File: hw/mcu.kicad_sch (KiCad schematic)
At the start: 40 parts, among them J3 Wisevision N114-2413THBIG01-H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, J4 Prog/debug, J5 Conn_02x04_Odd_Even, Q3 AO3401A, Q4 2N7002, Q5 2N7002, SW1 SW_Push_Shielded, SW2 SW_Push_Shielded, SW3 SW_Push_Shielded, SW8 SW_Push, U5 STM32L496RETx, U6 ZD25WQ16CTIGT, U7 PAM2804, Y1 32768 Hz

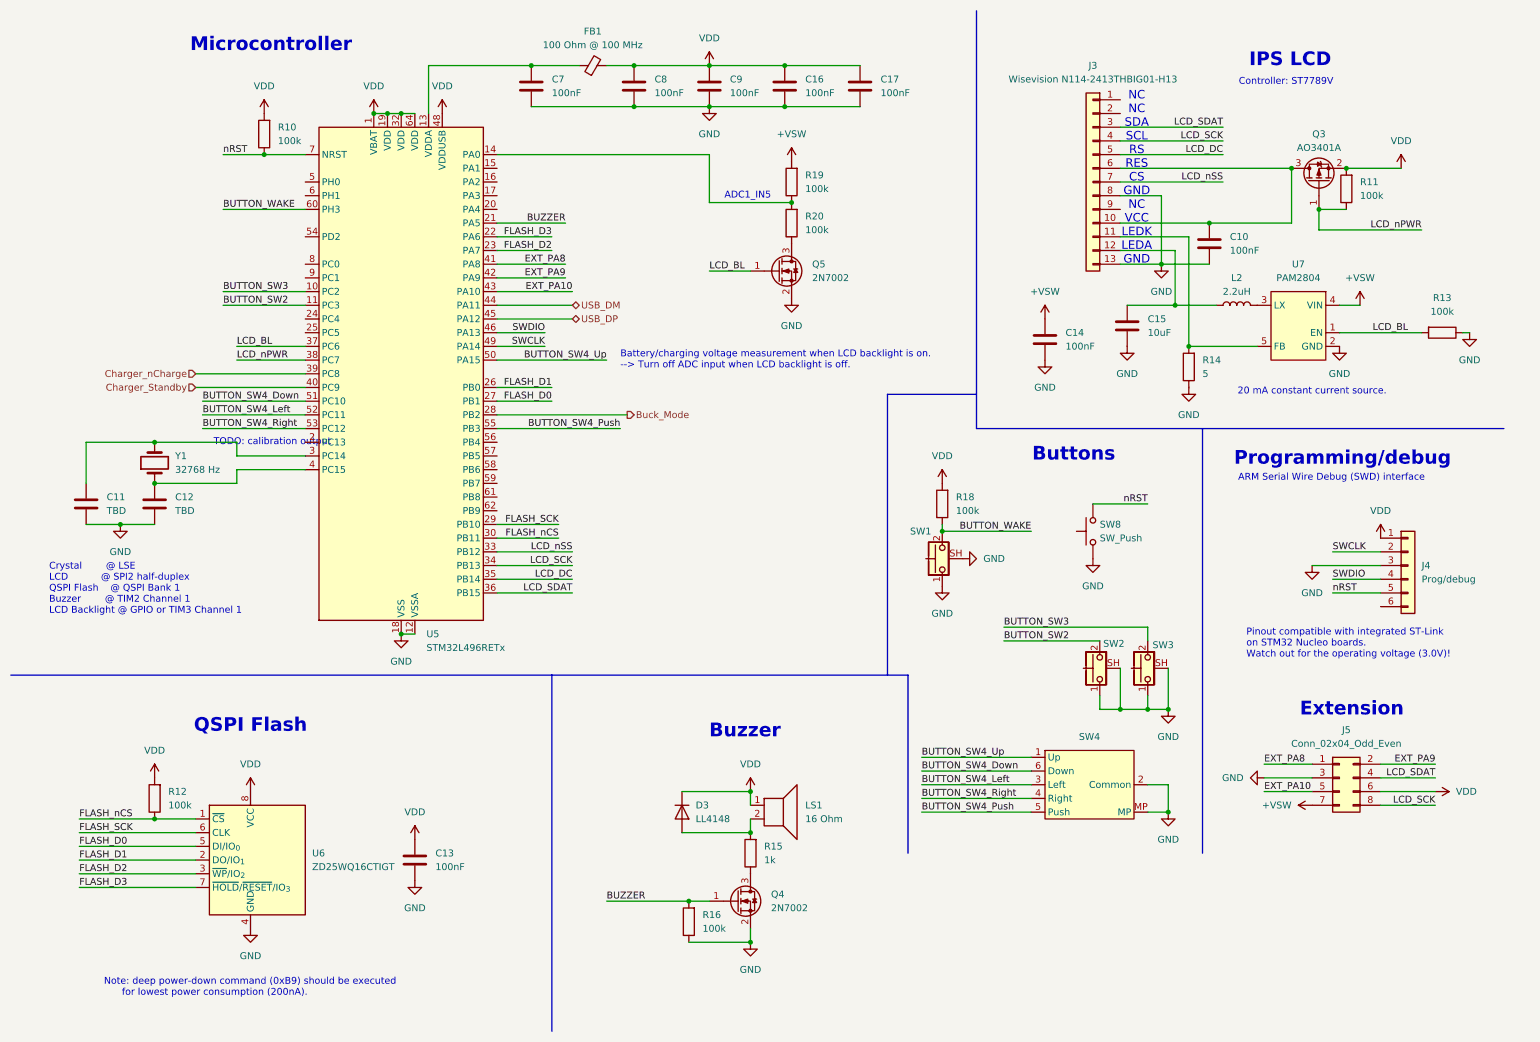
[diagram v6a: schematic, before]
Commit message: Placed remaining components.
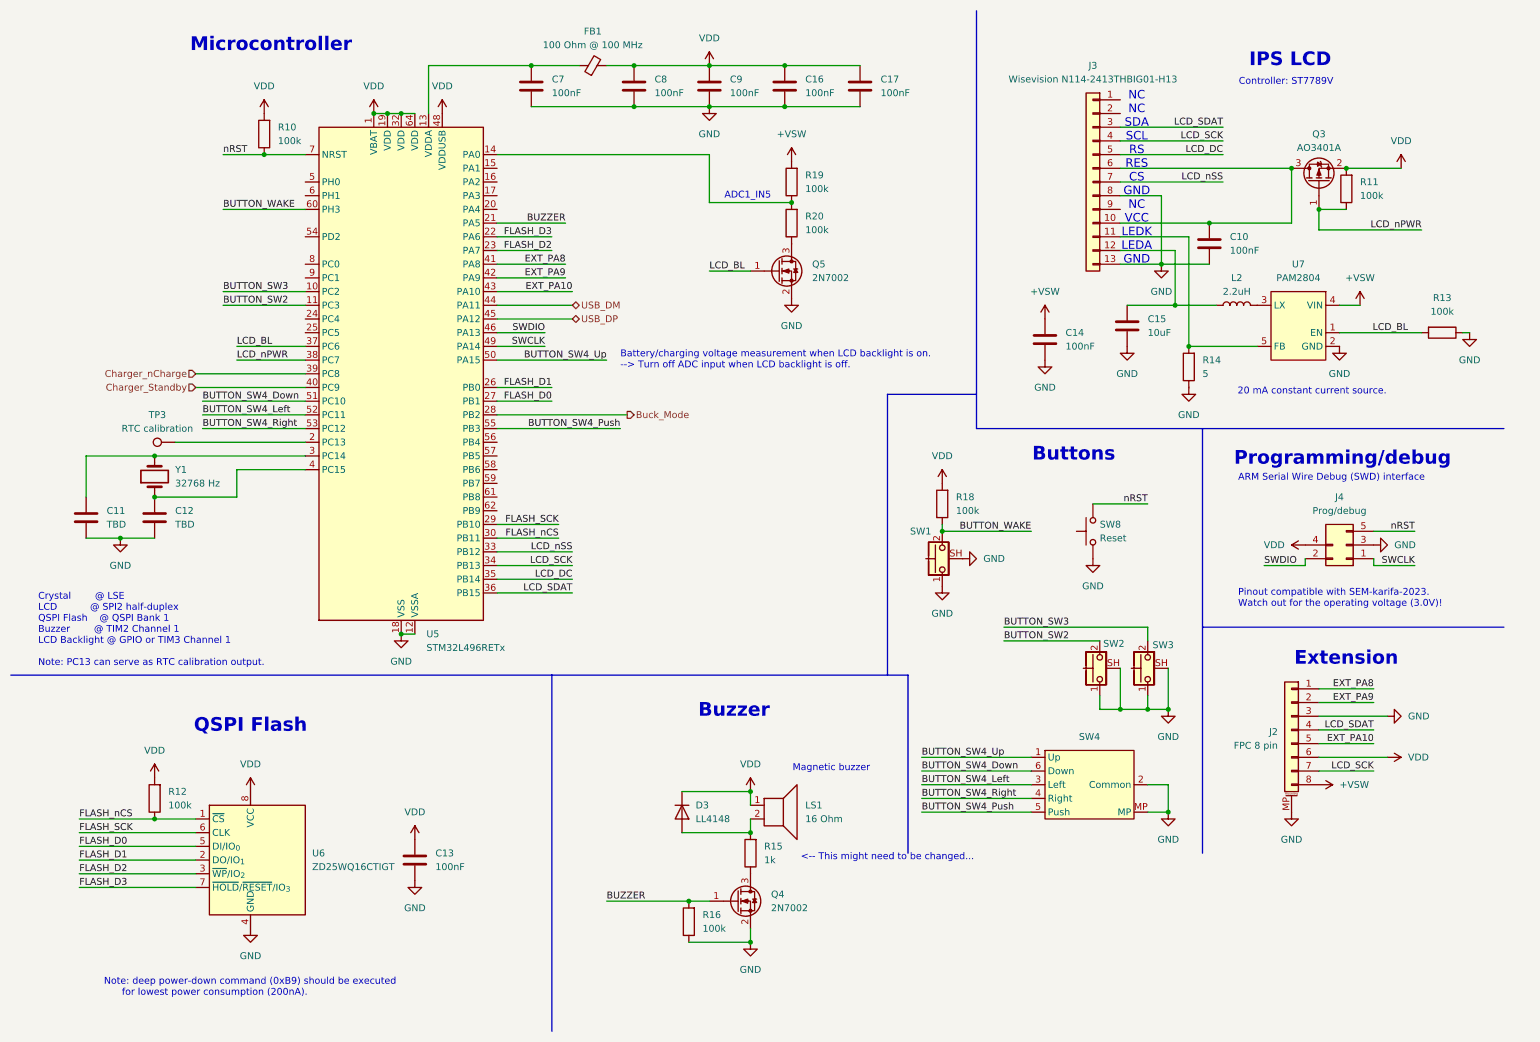
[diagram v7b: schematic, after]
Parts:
- removed J4: Prog/debug, Connector_PinHeader_2.54mm:PinHeader_1x06_P2.54mm_Vertical, symbol Connector_Generic:Conn_01x06
- removed J5: Conn_02x04_Odd_Even, Connector_PinHeader_2.54mm:PinHeader_2x04_P2.54mm_Vertical, symbol Connector_Generic:Conn_02x04_Odd_Even
- added J2: FPC 8 pin, Connector_FFC-FPC:Hirose_FH12-8S-0.5SH_1x08-1MP_P0.50mm_Horizontal, symbol Connector_Generic_MountingPin:Conn_01x08_MountingPin
- added J4: Prog/debug, sem18:ProgConnector_5pin, symbol Connector_Generic:Conn_2Rows-05Pins
- added TP3: RTC calibration, TestPoint:TestPoint_Pad_D1.0mm, symbol Connector:TestPoint
- LS1: footprint Buzzer_Beeper:MagneticBuzzer_CUI_CMT-8504-100-SMT -> sem18:Buzzer_8.5x8.5mm
- SW8: value SW_Push -> Reset; footprint (none) -> Button_Switch_SMD:SW_SPST_TL3342
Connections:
- net +VSW: now also J2.8 (Pin_8)
- net EXT_PA10: now also J2.5 (Pin_5)
- net EXT_PA8: now also J2.1 (Pin_1)
- net EXT_PA9: now also J2.2 (Pin_2)
- net GND: now also J2.3 (Pin_3), J2.MP (MountPin), J4.3 (Pin_3)
- net LCD_SCK: now also J2.7 (Pin_7)
- net LCD_SDAT: now also J2.4 (Pin_4)
- net SWCLK: now also J4.1 (Pin_1)
- net SWDIO: now also J4.2 (Pin_2)
- net VDD: now also J2.6 (Pin_6), J4.4 (Pin_4)
- net nRST: now also J4.5 (Pin_5)
- net at U5.2 (PC13): now also TP3.1
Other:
- note added: "<-- This might need to be changed..."
- note added: "Crystal @ LSE LCD @ SPI2 half-duplex QSPI Flash @ QSPI Bank 1 Buzzer @ TIM2 Channel 1 LCD Backlight @ GPIO or TIM3 Channel 1 Note: PC13 can serve as RTC calibration output."
- note added: "Magnetic buzzer"
- note added: "Pinout compatible with SEM-karifa-2023. Watch out for the operating voltage (3.0V)!"
- note removed: "Crystal @ LSE LCD @ SPI2 half-duplex QSPI Flash @ QSPI Bank 1 Buzzer @ TIM2 Channel 1 LCD Backlight @ GPIO or TIM3 Channel 1"
- note removed: "Pinout compatible with integrated ST-Link on STM32 Nucleo boards. Watch out for the operating voltage (3.0V)!"
- note removed: "TODO: calibration output"
- moved on the sheet: C11, C12, Y1

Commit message: Replaced extension connector.
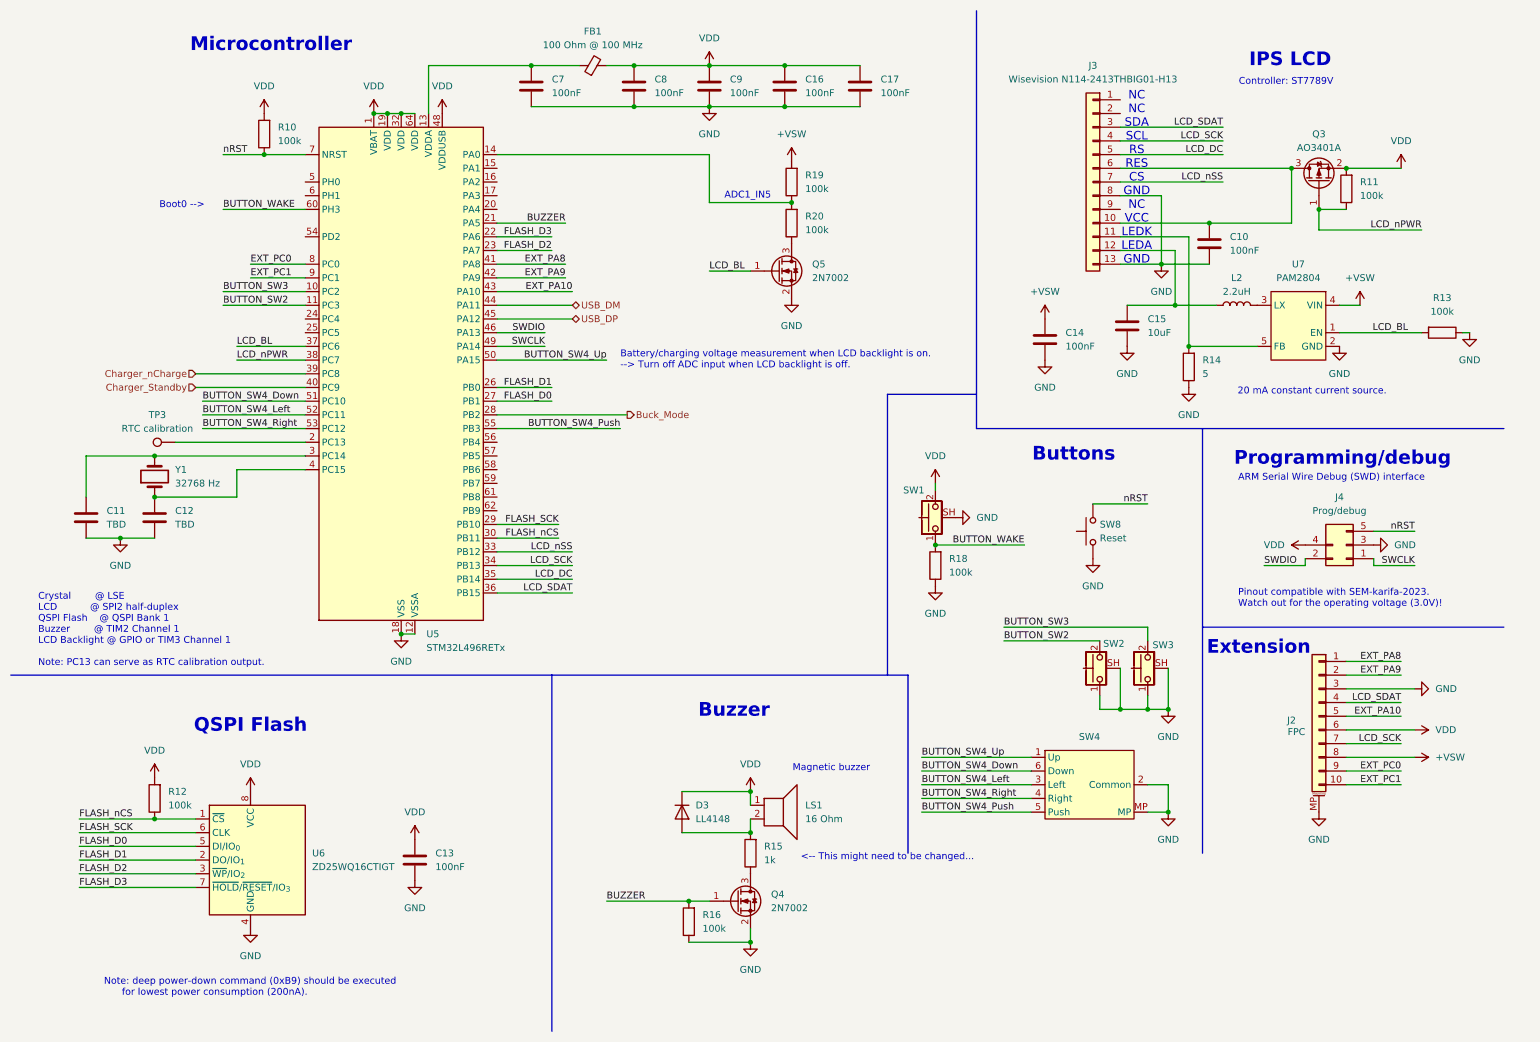
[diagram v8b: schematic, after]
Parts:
- removed J2: FPC 8 pin, Connector_FFC-FPC:Hirose_FH12-8S-0.5SH_1x08-1MP_P0.50mm_Horizontal, symbol Connector_Generic_MountingPin:Conn_01x08_MountingPin
- added J2: FPC, Connector_FFC-FPC:Hirose_FH12-10S-0.5SH_1x10-1MP_P0.50mm_Horizontal, symbol Connector_Generic_MountingPin:Conn_01x10_MountingPin
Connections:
- net +VSW: now also J2.8 (Pin_8)
- net BUTTON_WAKE: now also R18.2, SW1.1; no longer R18.1, SW1.2
- net EXT_PA10: now also J2.5 (Pin_5)
- net EXT_PA8: now also J2.1 (Pin_1)
- net EXT_PA9: now also J2.2 (Pin_2)
- net GND: now also R18.1, J2.3 (Pin_3), J2.MP (MountPin); no longer SW1.1
- net LCD_SCK: now also J2.7 (Pin_7)
- net LCD_SDAT: now also J2.4 (Pin_4)
- net VDD: now also SW1.2, J2.6 (Pin_6); no longer R18.2
- net EXT_PC0: now reaches U5.8 (PC0)
- net EXT_PC0: now also J2.9 (Pin_9)
- net EXT_PC1: now reaches U5.9 (PC1)
- net EXT_PC1: now also J2.10 (Pin_10)
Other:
- note added: "Boot0 -->"
- moved on the sheet: R18, SW1
